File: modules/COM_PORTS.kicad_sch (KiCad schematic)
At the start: 24 parts, among them J1 Conn_01x04, J2 Conn_01x04, J3 TC2030, J4 TC2030, J5 USB_C_Receptacle, J6 USB_C_Receptacle, U10 USBLC6-2SC6, U11 USBLC6-2SC6, U7 MAX40200AUK, U8 MAX40200AUK, U9 MAX40200AUK

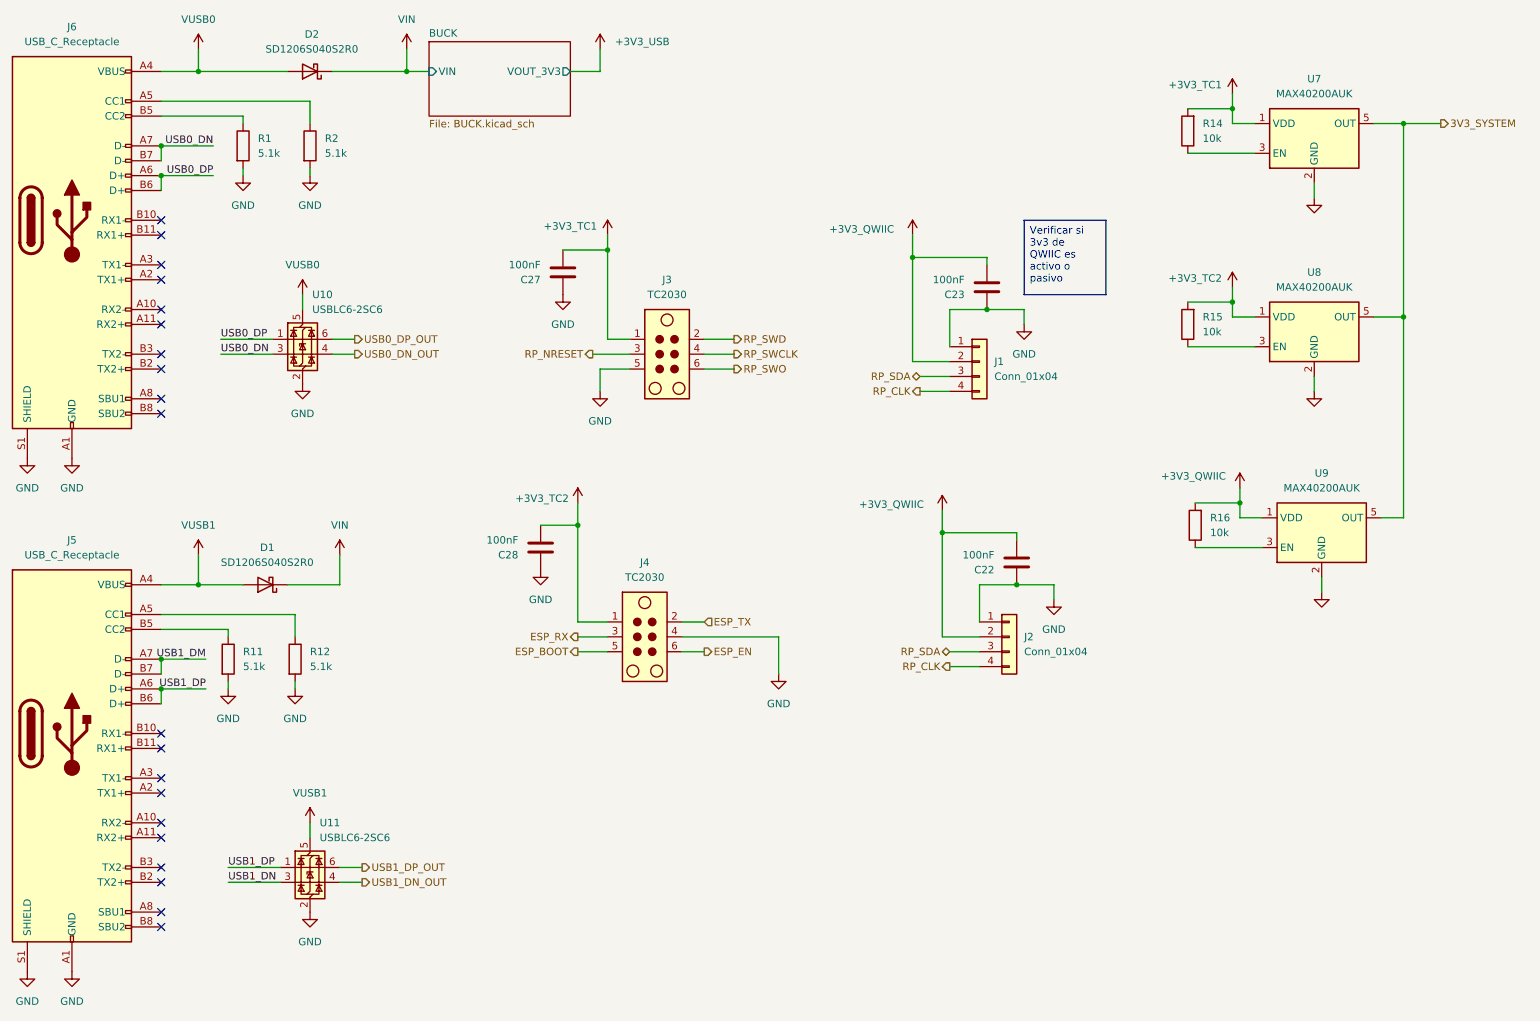
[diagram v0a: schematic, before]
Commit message: Adding mikroBUS
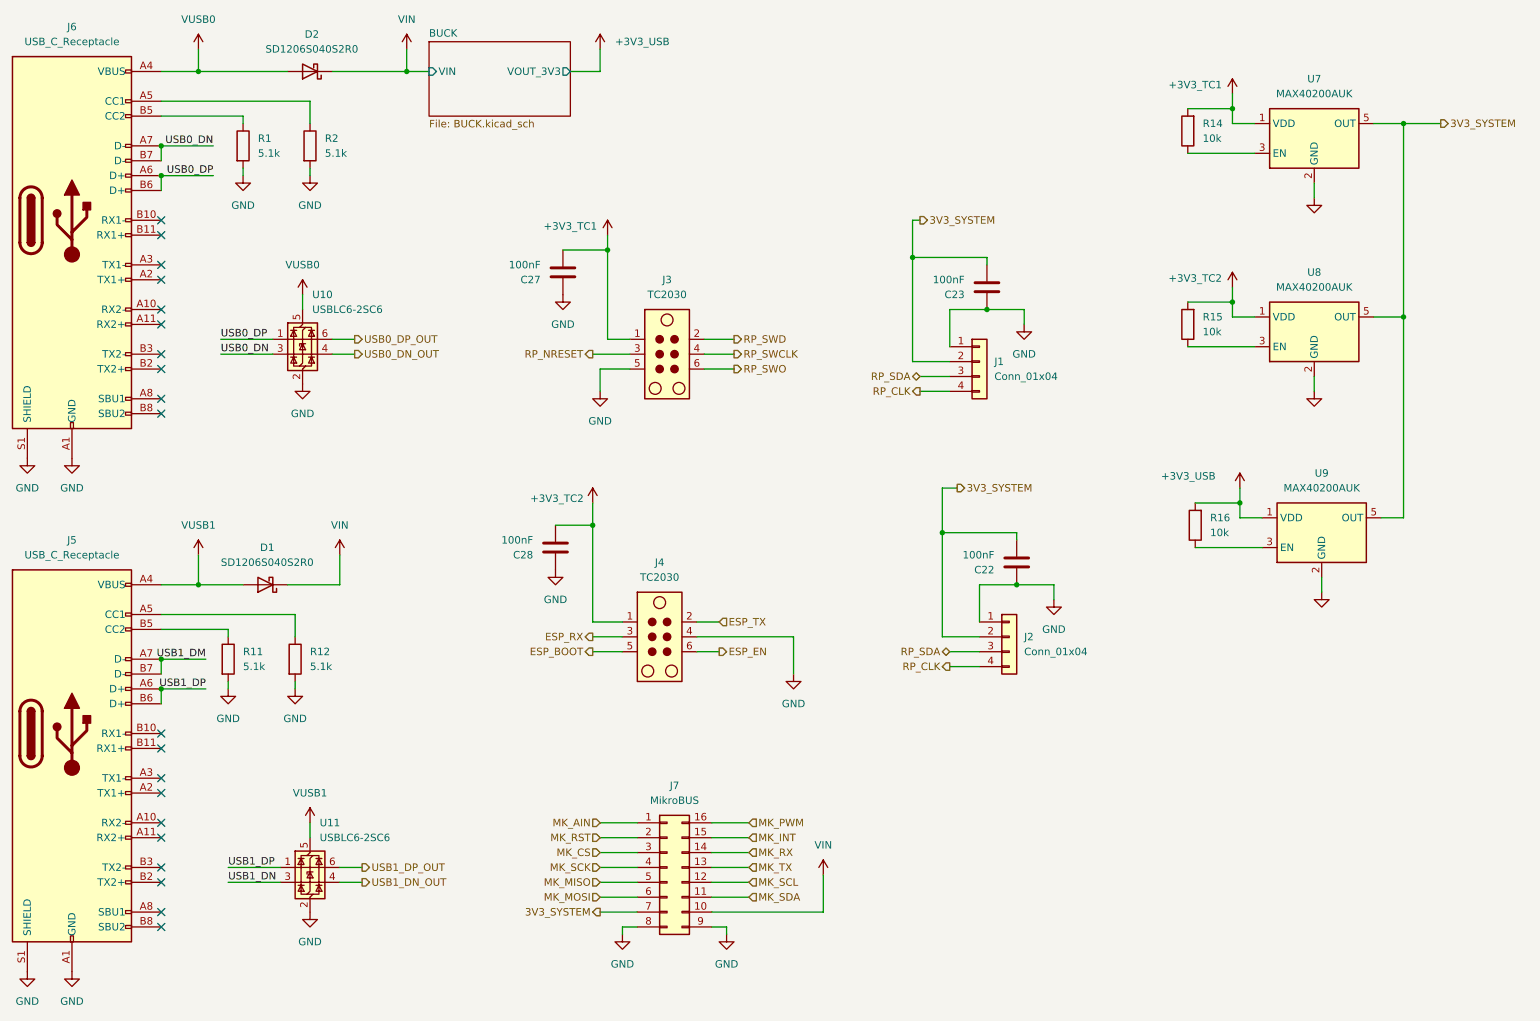
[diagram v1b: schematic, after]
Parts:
- added J7: MikroBUS, Sadman_connectors:MikroBUS, symbol Connector_Generic:Conn_02x08_Counter_Clockwise
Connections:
- net +3V3_USB: now also R16.2, U9.1 (VDD)
- net 3V3_SYSTEM: now also C22.2, C23.2, J1.2 (Pin_2), J2.2 (Pin_2), J7.7 (Pin_7)
- net GND: now also J7.8 (Pin_8), J7.9 (Pin_9)
- net VIN: now also J7.10 (Pin_10)
- removed net +3V3_QWIIC: C22.2, C23.2, J1.2 (Pin_2), J2.2 (Pin_2), R16.2, U9.1 (VDD)
- new net MK_AIN: J7.1 (Pin_1)
- new net MK_CS: J7.3 (Pin_3)
- new net MK_INT: J7.15 (Pin_15)
- new net MK_MISO: J7.5 (Pin_5)
- new net MK_MOSI: J7.6 (Pin_6)
- new net MK_PWM: J7.16 (Pin_16)
- new net MK_RST: J7.2 (Pin_2)
- new net MK_RX: J7.14 (Pin_14)
- new net MK_SCK: J7.4 (Pin_4)
- new net MK_SCL: J7.12 (Pin_12)
- new net MK_SDA: J7.11 (Pin_11)
- new net MK_TX: J7.13 (Pin_13)
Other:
- moved on the sheet: C28, J4

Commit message: Modificaciond de conexiones
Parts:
- removed C22, C23, C27, C28: 100nF, Capacitor_SMD:C_0402_1005Metric, symbol Device:C
- removed D1, D2: SD1206S040S2R0, Diode_SMD:D_1206_3216Metric, symbol Device:D_Schottky
- removed J1, J2: Conn_01x04, Connector_JST:JST_SH_BM04B-SRSS-TB_1x04-1MP_P1.00mm_Vertical, symbol Connector_Generic:Conn_01x04
- removed J3, J4: TC2030, Connector:Tag-Connect_TC2030-IDC-NL_2x03_P1.27mm_Vertical, symbol Connector:TC2030
- removed J5, J6: USB_C_Receptacle, Connector_USB:USB_C_Receptacle_Amphenol_12401610E4-2A, symbol Connector:USB_C_Receptacle
- removed J7: MikroBUS, Sadman_connectors:MikroBUS, symbol Connector_Generic:Conn_02x08_Counter_Clockwise
- removed R1, R11, R12, R2: 5.1k, Resistor_SMD:R_0603_1608Metric, symbol Device:R
- removed R14, R15, R16: 10k, Resistor_SMD:R_0603_1608Metric, symbol Device:R
- removed U10, U11: USBLC6-2SC6, Package_TO_SOT_SMD:SOT-23-6, symbol Power_Protection:USBLC6-2SC6
- removed U7, U8, U9: MAX40200AUK, Package_TO_SOT_SMD:SOT-23-5, symbol Analog_Switch:MAX40200AUK
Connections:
- no-connect marks 20 -> 0
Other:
- removed sheet BUCK
